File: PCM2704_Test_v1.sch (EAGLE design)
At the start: 39 parts, among them IC1 LT1963EFE-3.3, X1 USB-MB-S

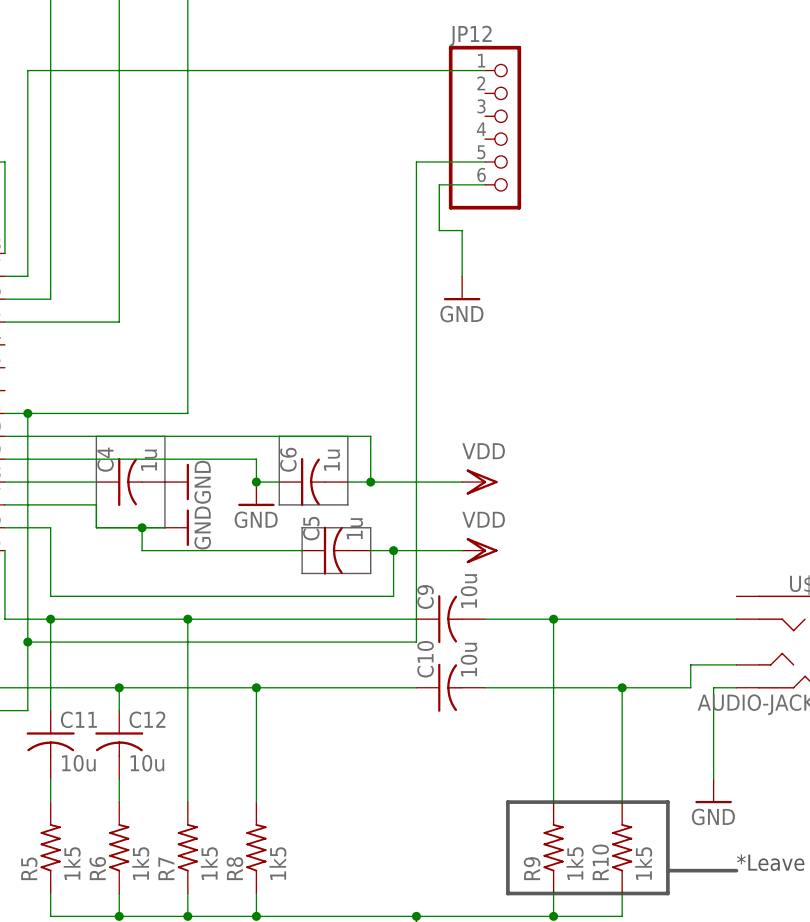
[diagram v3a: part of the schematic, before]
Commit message: Completed HP Traces
Completed the polygon pour for the headphone jack traces.
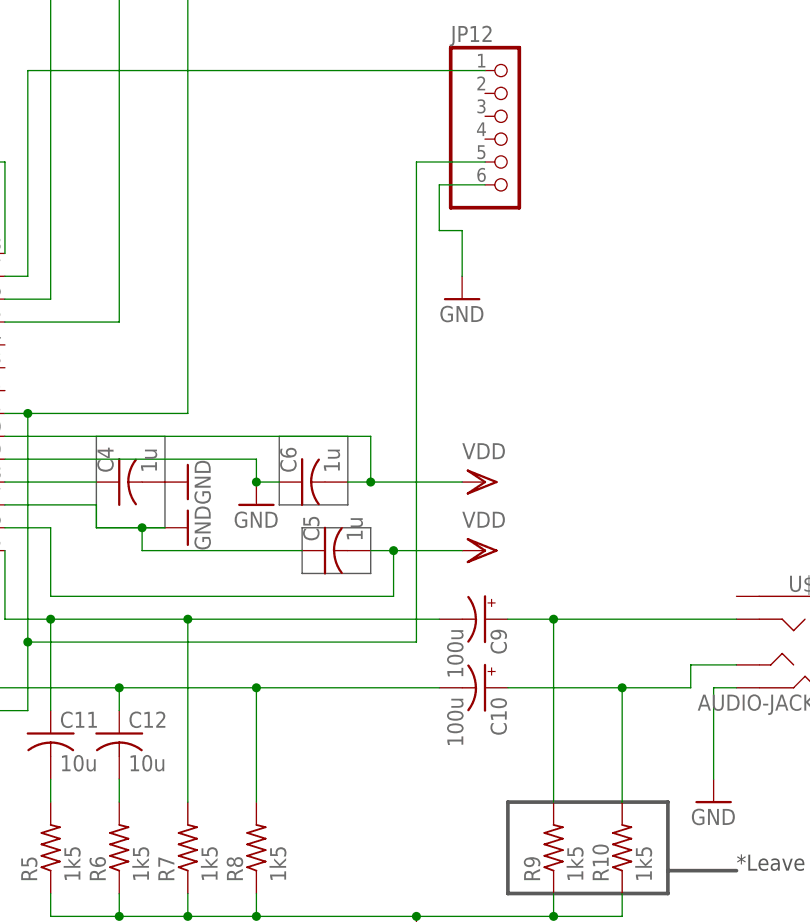
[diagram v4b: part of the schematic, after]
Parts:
- C10, C9: value 10u -> 100u; device rcl:C-USC0805 -> rcl:CPOL-USUD-8X10
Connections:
- net HP_OUT_L: now also C10.+; no longer C10.2
- net HP_OUT_R: now also C9.+; no longer C9.2
- net VOUTL: now also C10.-; no longer C10.1
- net VOUTR: now also C9.-; no longer C9.1
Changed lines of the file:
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@@
 <part name="R3" library="rcl" deviceset="R-US_" device="R0603" value="22"/>
 <part name="R4" library="rcl" deviceset="R-US_" device="R0603" value="22"/>
-<part name="C9" library="rcl" deviceset="C-US" device="C0805" value="10u"/>
-<part name="C10" library="rcl" deviceset="C-US" device="C0805" value="10u"/>
+<part name="C9" library="rcl" deviceset="CPOL-US" device="UD-8X10" value="100u"/>
+<part name="C10" library="rcl" deviceset="CPOL-US" device="UD-8X10" value="100u"/>
 <part name="C11" library="rcl" deviceset="C-US" device="C0805" value="10u"/>
 <part name="C12" library="rcl" deviceset="C-US" device="C0805" value="10u"/>
@@
 <instance part="R3" gate="G$1" x="-12.7" y="33.02"/>
 <instance part="R4" gate="G$1" x="-12.7" y="25.4"/>
-<instance part="C9" gate="G$1" x="160.02" y="17.78" rot="R90"/>
-<instance part="C10" gate="G$1" x="160.02" y="10.16" rot="R90"/>
+<instance part="C9" gate="G$1" x="165.1" y="17.78" rot="R270"/>
+<instance part="C10" gate="G$1" x="165.1" y="10.16" rot="R270"/>
 <instance part="C11" gate="G$1" x="116.84" y="5.08"/>
 <instance part="C12" gate="G$1" x="124.46" y="5.08"/>
@@
 <wire x1="104.14" y1="0" x2="104.14" y2="2.54" width="0.1524" layer="91"/>
 <junction x="104.14" y="2.54"/>
-<pinref part="JP12" gate="A" pin="5"/>
-<wire x1="165.1" y1="68.58" x2="157.48" y2="68.58" width="0.1524" layer="91"/>
-<wire x1="157.48" y1="68.58" x2="157.48" y2="15.24" width="0.1524" layer="91"/>
 <wire x1="157.48" y1="15.24" x2="114.3" y2="15.24" width="0.1524" layer="91"/>
 <junction x="114.3" y="15.24"/>
@@
 <wire x1="114.3" y1="40.64" x2="132.08" y2="40.64" width="0.1524" layer="91"/>
 <wire x1="132.08" y1="40.64" x2="132.08" y2="96.52" width="0.1524" layer="91"/>
+<pinref part="JP12" gate="A" pin="5"/>
+<wire x1="165.1" y1="68.58" x2="157.48" y2="68.58" width="0.1524" layer="91"/>
+<wire x1="157.48" y1="15.24" x2="157.48" y2="68.58" width="0.1524" layer="91"/>
 </segment>
 </net>
@@
 <wire x1="111.76" y1="25.4" x2="111.76" y2="17.78" width="0.1524" layer="91"/>
 <wire x1="111.76" y1="17.78" x2="116.84" y2="17.78" width="0.1524" layer="91"/>
-<pinref part="C9" gate="G$1" pin="1"/>
 <pinref part="R7" gate="G$1" pin="2"/>
 <wire x1="116.84" y1="17.78" x2="132.08" y2="17.78" width="0.1524" layer="91"/>
-<wire x1="132.08" y1="17.78" x2="157.48" y2="17.78" width="0.1524" layer="91"/>
 <wire x1="132.08" y1="-2.54" x2="132.08" y2="17.78" width="0.1524" layer="91"/>
-<junction x="132.08" y="17.78"/>
 <pinref part="C11" gate="G$1" pin="1"/>
 <wire x1="116.84" y1="7.62" x2="116.84" y2="17.78" width="0.1524" layer="91"/>
 <junction x="116.84" y="17.78"/>
+<pinref part="C9" gate="G$1" pin="-"/>
+<wire x1="132.08" y1="17.78" x2="160.02" y2="17.78" width="0.1524" layer="91"/>
+<junction x="132.08" y="17.78"/>
 </segment>
 </net>
@@
 <wire x1="50.8" y1="25.4" x2="50.8" y2="10.16" width="0.1524" layer="91"/>
 <wire x1="50.8" y1="10.16" x2="124.46" y2="10.16" width="0.1524" layer="91"/>
-<pinref part="C10" gate="G$1" pin="1"/>
 <pinref part="R8" gate="G$1" pin="2"/>
 <wire x1="124.46" y1="10.16" x2="139.7" y2="10.16" width="0.1524" layer="91"/>
-<wire x1="139.7" y1="10.16" x2="157.48" y2="10.16" width="0.1524" layer="91"/>
 <wire x1="139.7" y1="-2.54" x2="139.7" y2="10.16" width="0.1524" layer="91"/>
-<junction x="139.7" y="10.16"/>
 <pinref part="C12" gate="G$1" pin="1"/>
 <wire x1="124.46" y1="7.62" x2="124.46" y2="10.16" width="0.1524" layer="91"/>
 <junction x="124.46" y="10.16"/>
+<pinref part="C10" gate="G$1" pin="-"/>
+<wire x1="139.7" y1="10.16" x2="160.02" y2="10.16" width="0.1524" layer="91"/>
+<junction x="139.7" y="10.16"/>
 </segment>
 </net>
 <net name="HP_OUT_R" class="0">
 <segment>
-<pinref part="C9" gate="G$1" pin="2"/>
-<wire x1="165.1" y1="17.78" x2="172.72" y2="17.78" width="0.1524" layer="91"/>
 <pinref part="R9" gate="G$1" pin="2"/>
 <wire x1="172.72" y1="17.78" x2="193.04" y2="17.78" width="0.1524" layer="91"/>
 <wire x1="172.72" y1="-2.54" x2="172.72" y2="17.78" width="0.1524" layer="91"/>
+<pinref part="U$2" gate="G$1" pin="RING1"/>
+<pinref part="C9" gate="G$1" pin="+"/>
+<wire x1="167.64" y1="17.78" x2="172.72" y2="17.78" width="0.1524" layer="91"/>
 <junction x="172.72" y="17.78"/>
-<pinref part="U$2" gate="G$1" pin="RING1"/>
 </segment>
 </net>
 <net name="HP_OUT_L" class="0">
 <segment>
-<pinref part="C10" gate="G$1" pin="2"/>
-<wire x1="165.1" y1="10.16" x2="180.34" y2="10.16" width="0.1524" layer="91"/>
 <pinref part="R10" gate="G$1" pin="2"/>
 <wire x1="180.34" y1="10.16" x2="187.96" y2="10.16" width="0.1524" layer="91"/>
 <wire x1="180.34" y1="-2.54" x2="180.34" y2="10.16" width="0.1524" layer="91"/>
-<junction x="180.34" y="10.16"/>
 <wire x1="187.96" y1="10.16" x2="187.96" y2="12.7" width="0.1524" layer="91"/>
 <pinref part="U$2" gate="G$1" pin="TIP"/>
 <wire x1="187.96" y1="12.7" x2="193.04" y2="12.7" width="0.1524" layer="91"/>
-</segment>
-</net>
+<pinref part="C10" gate="G$1" pin="+"/>
+<wire x1="167.64" y1="10.16" x2="180.34" y2="10.16" width="0.1524" layer="91"/>
+<junction x="180.34" y="10.16"/>
+</segment>
+</net>

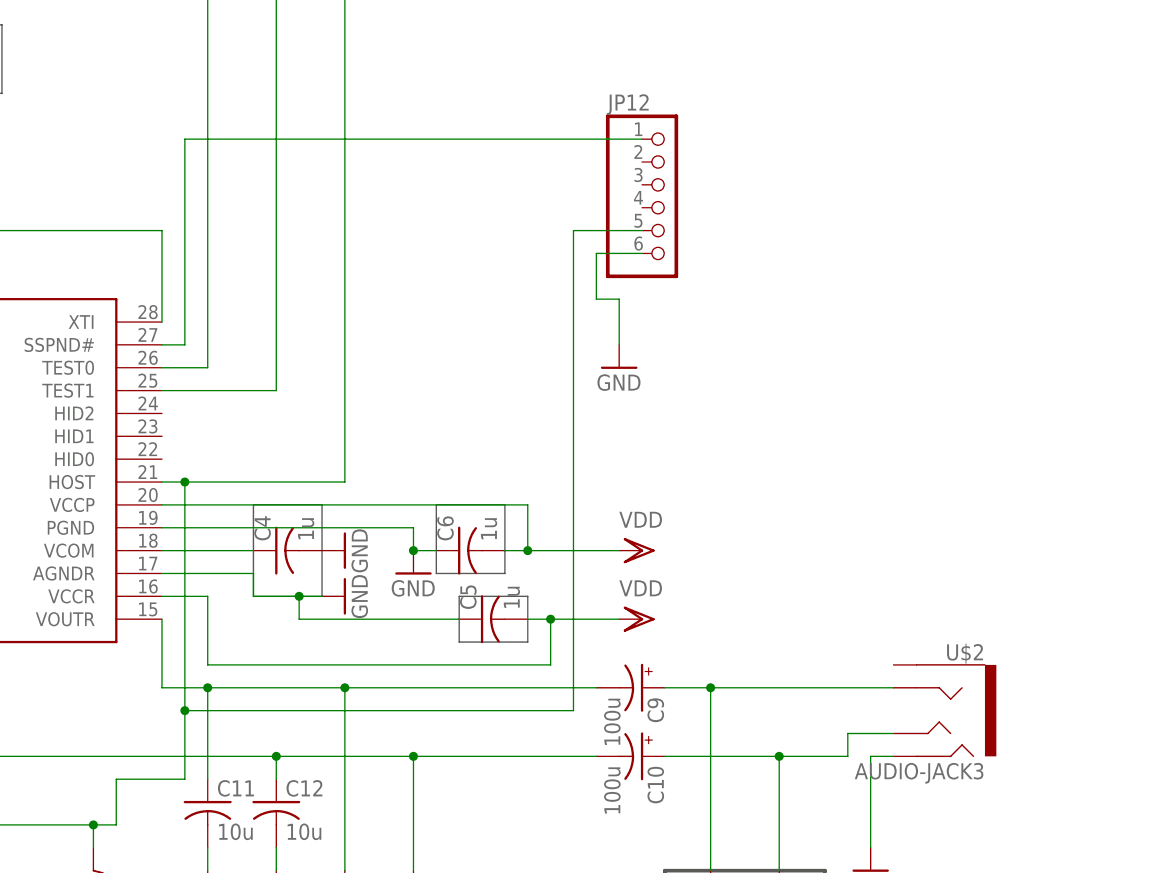
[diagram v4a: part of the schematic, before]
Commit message: Ran power traces
Ran power traces and moves some components to make room for the power.
Rearranged some resistors to optimize the layout.
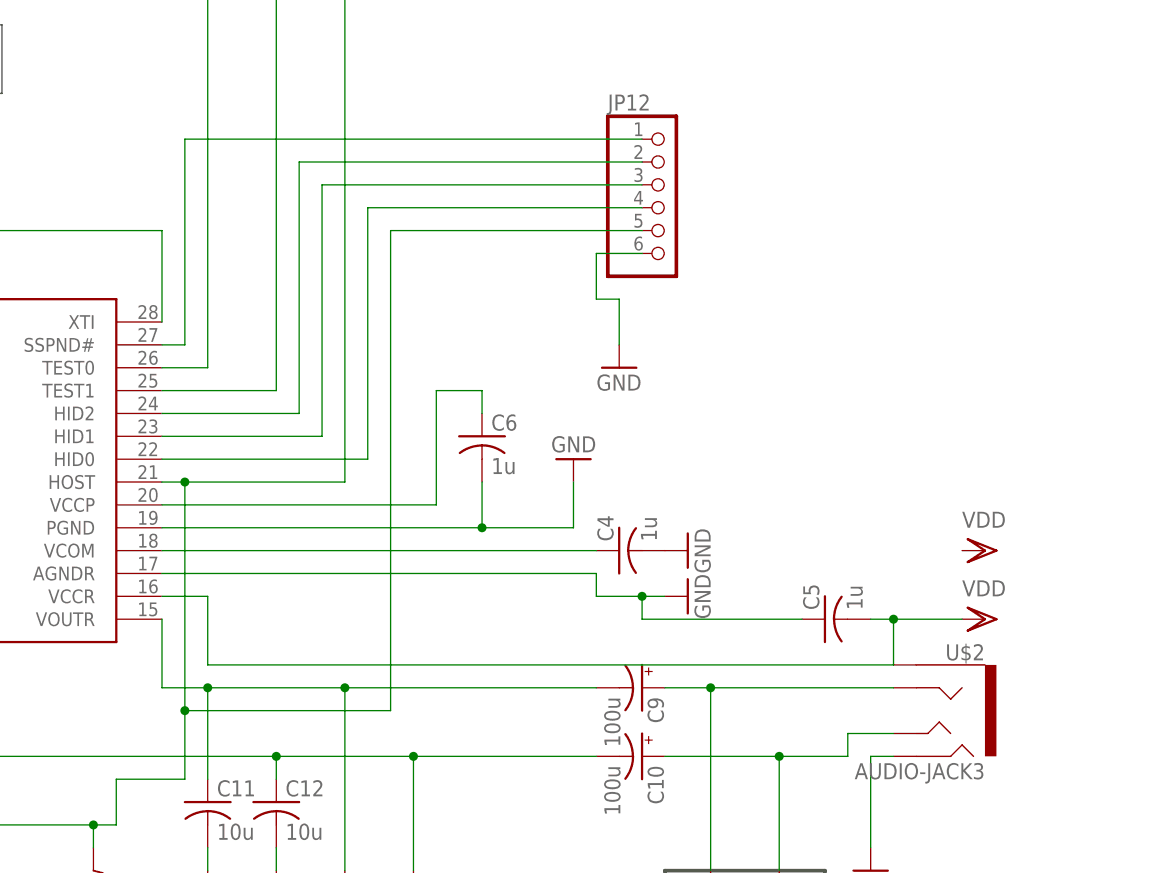
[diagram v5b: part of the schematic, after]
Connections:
- new net N$4: JP12.2, U$1.HID2
- new net N$6: JP12.3, U$1.HID1
- new net N$7: JP12.4, U$1.HID0
- new net N$9: C6.1, U$1.VCCP
- net GND: now also C6.2; no longer C6.1
- net VDD: no longer C6.2, U$1.VCCP
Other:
- moved on the sheet: C4, C5, C6

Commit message: Completed Board
The board is now complete and ready for printing as soon as it is
reviewed.
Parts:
- added C14: 10u, rc-master-smd:CP_SV-D
- added C15: 100n, rc-master-smd:C_0805
- L1: value (none) -> 10uH
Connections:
- net GND: now also C14.-, C15.1
- net VDD: now also C14.+, C15.2
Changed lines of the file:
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@@
 <part name="U$2" library="SparkFun-Connectors" deviceset="AUDIO-JACK3" device=""/>
 <part name="GND8" library="SparkFun" deviceset="GND" device=""/>
-<part name="L1" library="rcl" deviceset="L-US" device="L3225M"/>
+<part name="L1" library="rcl" deviceset="L-US" device="L3225M" value="10uH"/>
 <part name="R2" library="rcl" deviceset="R-US_" device="R0603" value="1k5"/>
 <part name="GND16" library="SparkFun" deviceset="GND" device=""/>
@@
 <part name="GND10" library="SparkFun" deviceset="GND" device=""/>
 <part name="GND6" library="SparkFun" deviceset="GND" device=""/>
+<part name="C14" library="rc-master-smd" deviceset="CP_" device="SV-D" value="10u"/>
+<part name="GND11" library="SparkFun" deviceset="GND" device=""/>
+<part name="C15" library="rc-master-smd" deviceset="C_" device="0805" value="100n"/>
+<part name="GND12" library="SparkFun" deviceset="GND" device=""/>
 </parts>
 <sheets>
@@
 <instance part="GND10" gate="1" x="-43.18" y="-12.7" rot="R90"/>
 <instance part="GND6" gate="1" x="157.48" y="43.18" rot="R180"/>
+<instance part="C14" gate="G$1" x="-35.56" y="5.08" rot="R90"/>
+<instance part="GND11" gate="1" x="-35.56" y="0"/>
+<instance part="C15" gate="G$1" x="-27.94" y="5.08" rot="R90"/>
+<instance part="GND12" gate="1" x="-27.94" y="0"/>
 </instances>
 <busses>
@@
 <wire x1="157.48" y1="35.56" x2="157.48" y2="40.64" width="0.1524" layer="91"/>
 <junction x="147.32" y="35.56"/>
+</segment>
+<segment>
+<pinref part="C14" gate="G$1" pin="-"/>
+<pinref part="GND11" gate="1" pin="GND"/>
+</segment>
+<segment>
+<pinref part="C15" gate="G$1" pin="1"/>
+<pinref part="GND12" gate="1" pin="GND"/>
 </segment>
 </net>
@@
 <pinref part="VDD1" gate="G$1" pin="VDD"/>
 <pinref part="IC1" gate="G$1" pin="OUT@3"/>
-<wire x1="-40.64" y1="10.16" x2="-25.4" y2="10.16" width="0.1524" layer="91"/>
+<wire x1="-40.64" y1="10.16" x2="-35.56" y2="10.16" width="0.1524" layer="91"/>
+<wire x1="-35.56" y1="10.16" x2="-27.94" y2="10.16" width="0.1524" layer="91"/>
+<wire x1="-27.94" y1="10.16" x2="-25.4" y2="10.16" width="0.1524" layer="91"/>
 <wire x1="-43.18" y1="5.08" x2="-40.64" y2="5.08" width="0.1524" layer="91"/>
 <wire x1="-40.64" y1="5.08" x2="-40.64" y2="7.62" width="0.1524" layer="91"/>
@@
 <wire x1="-43.18" y1="7.62" x2="-40.64" y2="7.62" width="0.1524" layer="91"/>
 <junction x="-40.64" y="7.62"/>
+<pinref part="C14" gate="G$1" pin="+"/>
+<wire x1="-35.56" y1="7.62" x2="-35.56" y2="10.16" width="0.1524" layer="91"/>
+<junction x="-35.56" y="10.16"/>
+<pinref part="C15" gate="G$1" pin="2"/>
+<wire x1="-27.94" y1="7.62" x2="-27.94" y2="10.16" width="0.1524" layer="91"/>
+<junction x="-27.94" y="10.16"/>
 </segment>
 </net>
